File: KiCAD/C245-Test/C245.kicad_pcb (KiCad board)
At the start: 4 copper layers, 28 x 30 mm, 63 parts, among them J1 USB_C_Receptacle_USB2.0, J2 OLED_64x32, J3 C245, J5 DNP, Q1 SS8050, Q2 DMP3017SFG, SW1 key1, SW2 key2, U1 USBLC6-4SC6, U2 AP2204R-3.3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

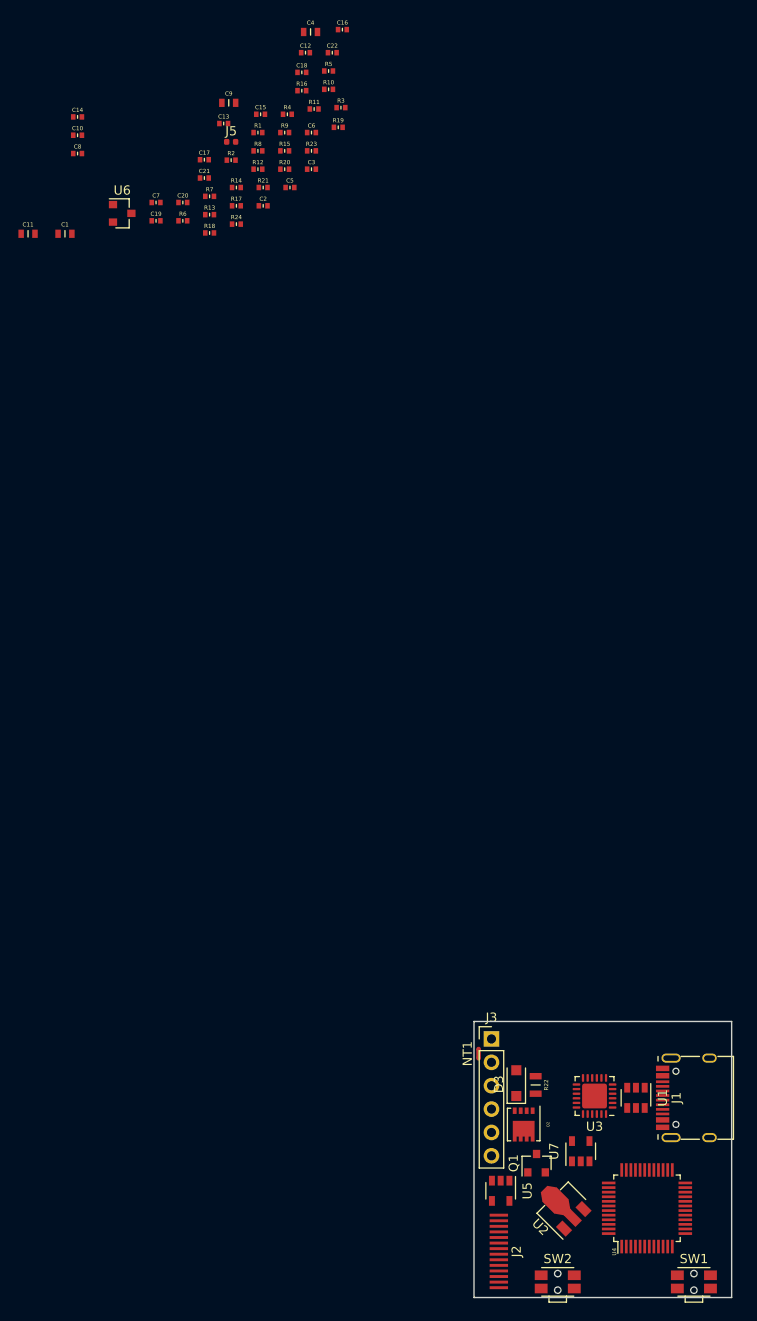
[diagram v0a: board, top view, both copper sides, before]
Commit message: added C245_Test
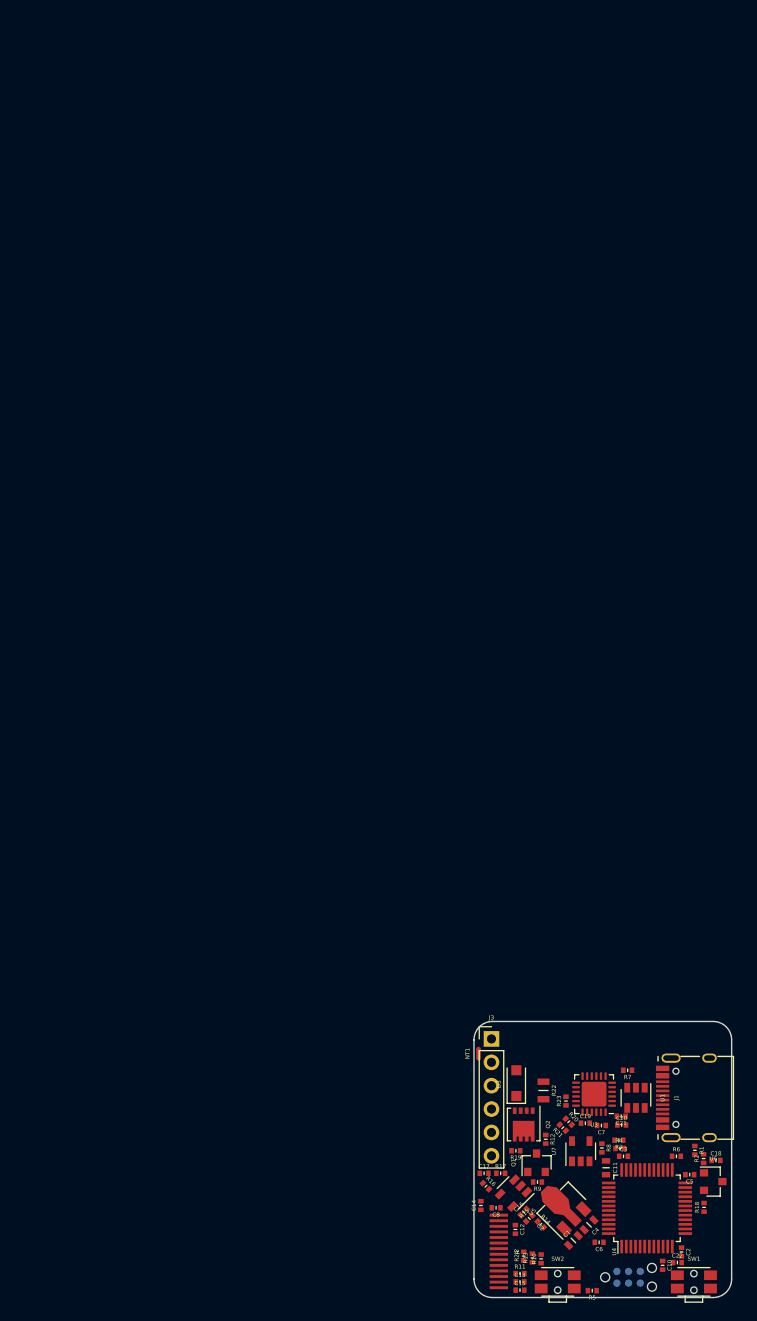
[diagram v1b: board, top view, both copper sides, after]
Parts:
- removed C9: 1μF 25V, otter:C_0603
- removed J5: DNP, Resistor_SMD:R_0402_1005Metric
- added P1: TC2030-CTX, otter:TC2030, B.Cu at (102.8, 117.8)
- moved C10 138.3 mm to (106.5, 116.5), turned to 270 degrees
- moved C22 136.7 mm to (108.1, 116.2)
- moved R5 135.6 mm to (98.8, 119.2), turned to 180 degrees
- moved C4 133.1 mm to (98.5, 112.1), turned to 225 degrees
- moved C15 130.9 mm to (91.0, 119.2)
- moved C16 130.0 mm to (91.4, 110.7), turned to 45 degrees
- moved C13 129.9 mm to (91.0, 118.3)
- moved C12 129.9 mm to (90.5, 112.6), turned to 270 degrees
- moved R10 129.2 mm to (93.3, 115.8), turned to 90 degrees
- moved R11 128.5 mm to (91.0, 117.4)
- moved C18 126.5 mm to (112.3, 105.1)
- moved C14 126.2 mm to (86.8, 110.0), turned to 90 degrees
- moved C6 124.6 mm to (99.6, 114.0), turned to 180 degrees
- moved U6 123.3 mm to (112.0, 107.4)
- moved C8 123.3 mm to (88.4, 110.2), turned to 180 degrees
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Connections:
- R5 pad 2: Net-(J5-Pad1) -> Net-(R5-Pad2)
- SW2 pad 2: Net-(SW2-Pad2) -> Net-(R5-Pad2)
- U4 pad 14: Net-(SW2-Pad2) -> Net-(U4-Pad14)
- U4 pad 2: Net-(U4-Pad2) -> Net-(R5-Pad2)
- U4 pad 44: Net-(J5-Pad1) -> Net-(R5-Pad2)
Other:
- outline, holes or cut-outs redrawn

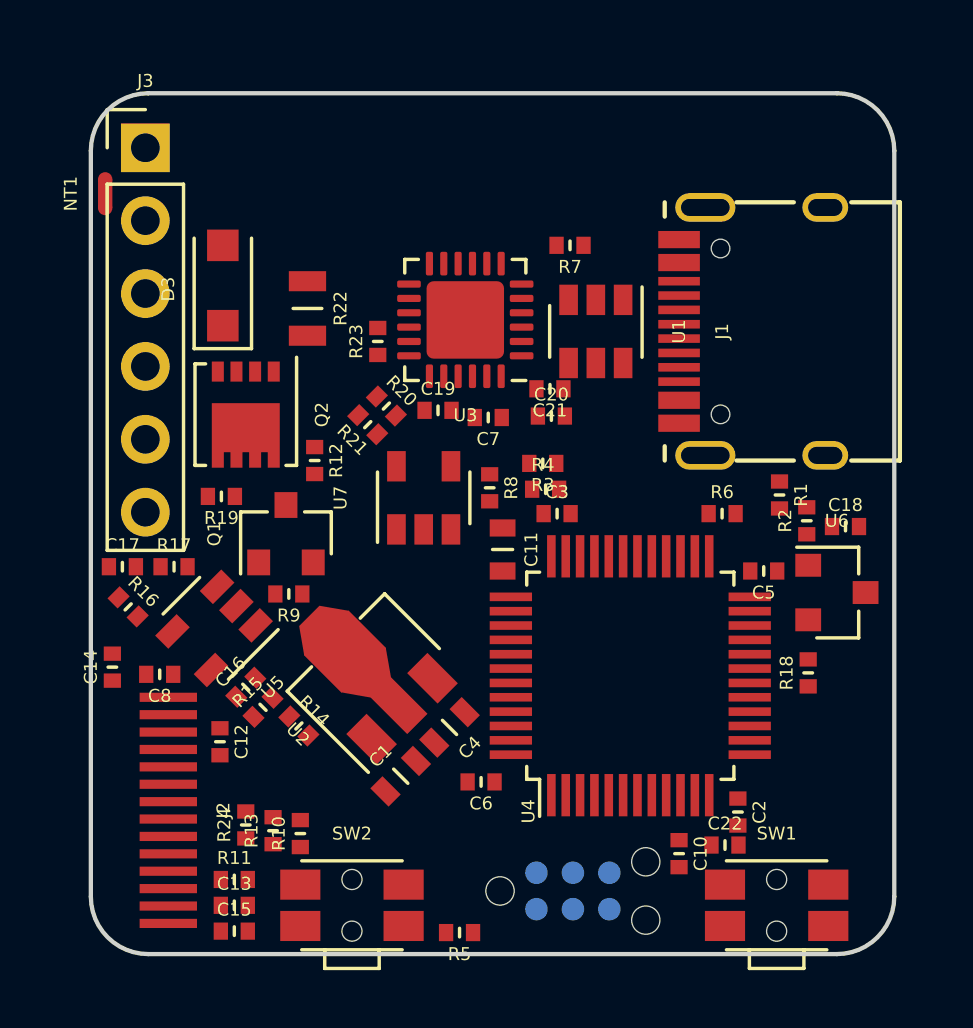
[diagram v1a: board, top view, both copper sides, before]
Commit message: added C245_Test
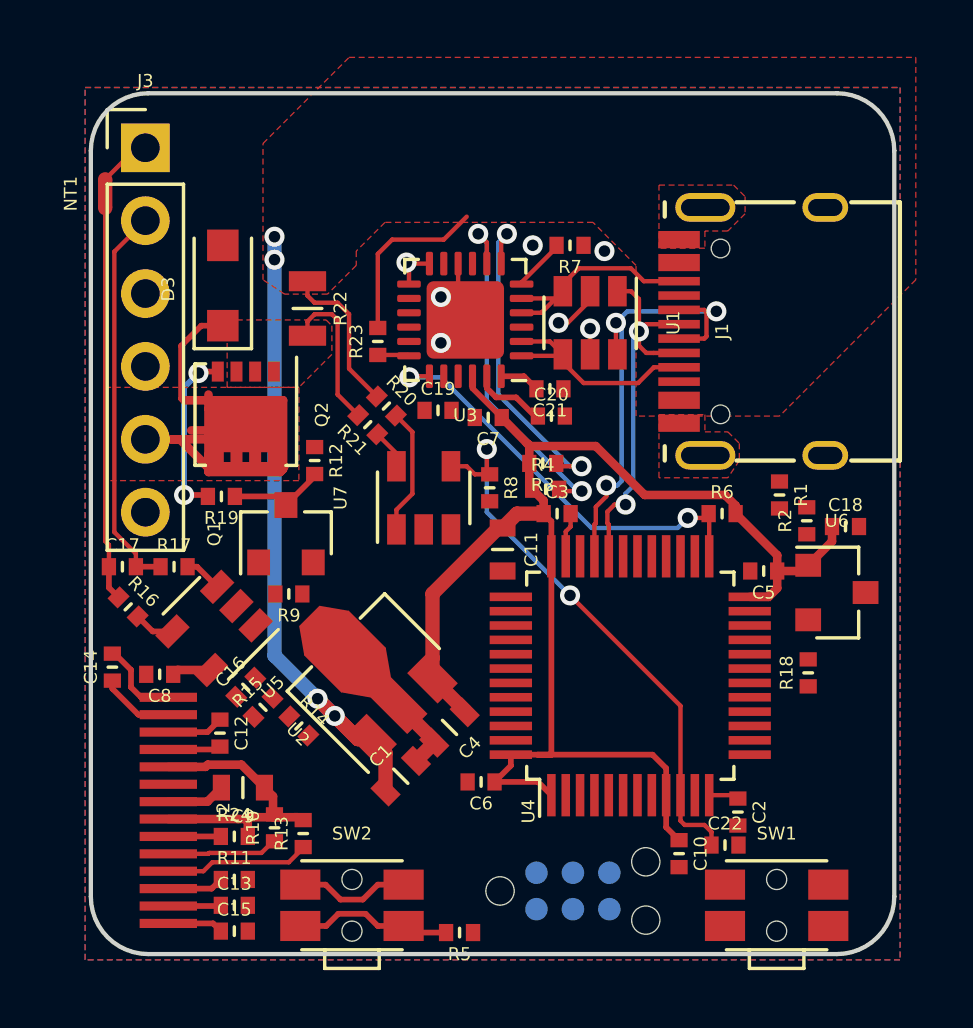
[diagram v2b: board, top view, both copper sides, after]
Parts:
- added C9: 1μF 25V, otter:C_0603, F.Cu at (91.3, 114.2)
- moved R13 1.05 mm to (93.4, 115.8)
- moved R10 0.92 mm to (92.4, 115.6)
- moved R24 0.57 mm to (91.0, 115.9), turned to 0 degrees
- moved U1 0.36 mm to (103.4, 98.0)
- moved C12 0.30 mm to (90.5, 112.3)
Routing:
- net +3V3: track 0.00 -> 68.1 mm, vias 0 -> 1
- net VBUS: track 0.00 -> 36.3 mm, vias 0 -> 4
- net Net-(D3-Pad1): track 0.00 -> 26.4 mm
- net IIN: track 0.00 -> 19.8 mm, vias 0 -> 2
- net USB_P: track 0.00 -> 16.8 mm, vias 0 -> 3
- net INT_N: track 0.00 -> 15.0 mm, vias 0 -> 2
- net USB_N: track 0.00 -> 14.0 mm, vias 0 -> 2
- net Net-(C17-Pad1): track 0.00 -> 13.8 mm
- net C245_JUNC: track 0.00 -> 13.7 mm
- net GND: track 0.00 -> 13.6 mm, vias 0 -> 6
- net SDA: track 0.00 -> 12.5 mm, vias 0 -> 2
- net SCL: track 0.00 -> 11.7 mm, vias 0 -> 2
- net CC2: track 0.00 -> 8.00 mm
- net CC1: track 0.00 -> 7.94 mm
- net Net-(Q2-Pad4): track 0.00 -> 6.00 mm, vias 0 -> 2
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- added copper zone on B.Cu, net GND
- added copper zone on F.Cu, net GND
- added copper zone on F.Cu, net Net-(D3-Pad1)
- added copper zone on F.Cu, net Net-(Q2-Pad1)
- added copper zone on F.Cu, net VBUS
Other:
- copper layers 4 -> 2

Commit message: finished routing C245_Test
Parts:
- moved R24 0.30 mm to (91.0, 115.6)
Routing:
- net +3V3: track 68.1 -> 100.0 mm, vias 1 -> 6
- net TTIP: track 0.00 -> 24.1 mm, vias 0 -> 2
- net SWCLK: track 0.00 -> 16.7 mm, vias 0 -> 1
- net PWM: track 0.00 -> 15.3 mm, vias 0 -> 2
- net SWDIO: track 0.00 -> 14.5 mm, vias 0 -> 1
- net VBUS: track 36.3 -> 50.3 mm, vias 4 -> 7
- net Net-(SW1-Pad2): track 0.00 -> 13.2 mm
- net Net-(R5-Pad2): track 5.53 -> 18.2 mm, vias 0 -> 2
- net UIN: track 1.05 -> 13.6 mm, vias 0 -> 2
- net OLED_SCL: track 3.88 -> 16.3 mm, vias 0 -> 2
- net OLED_SDA: track 5.07 -> 14.8 mm, vias 0 -> 2
- net SCL: track 11.7 -> 21.3 mm, vias 2 -> 3
- net SDA: track 12.5 -> 21.0 mm, vias 2 -> 3
- net Net-(C16-Pad1): track 1.43 -> 6.34 mm
- net GND: track 13.6 -> 18.2 mm, vias 6 -> 55
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
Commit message: finalized design
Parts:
- added G***: LOGO, otter:C245_silk, F.Cu at (98.4, 92.7)
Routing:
- net GND: vias 55 -> 56

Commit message: added silkscreen
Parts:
- moved G*** 0.56 mm to (97.8, 92.5)
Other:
- board text added: "*mau*"

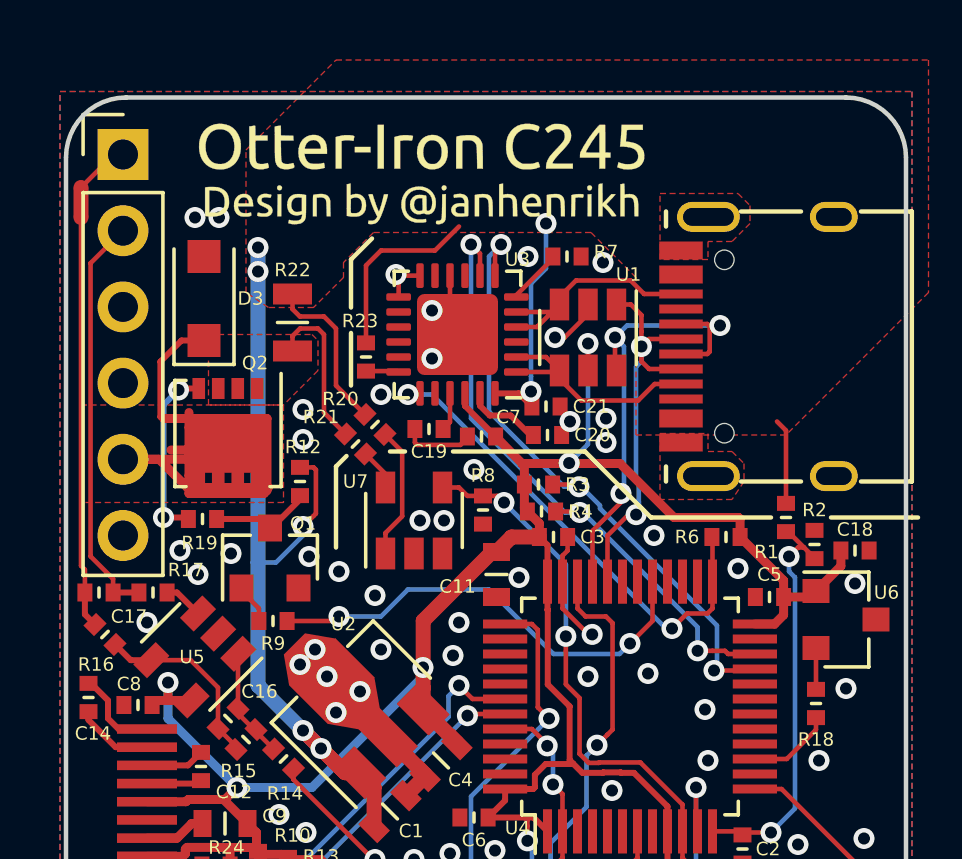
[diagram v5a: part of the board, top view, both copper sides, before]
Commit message: added connector pcb, added Gerber
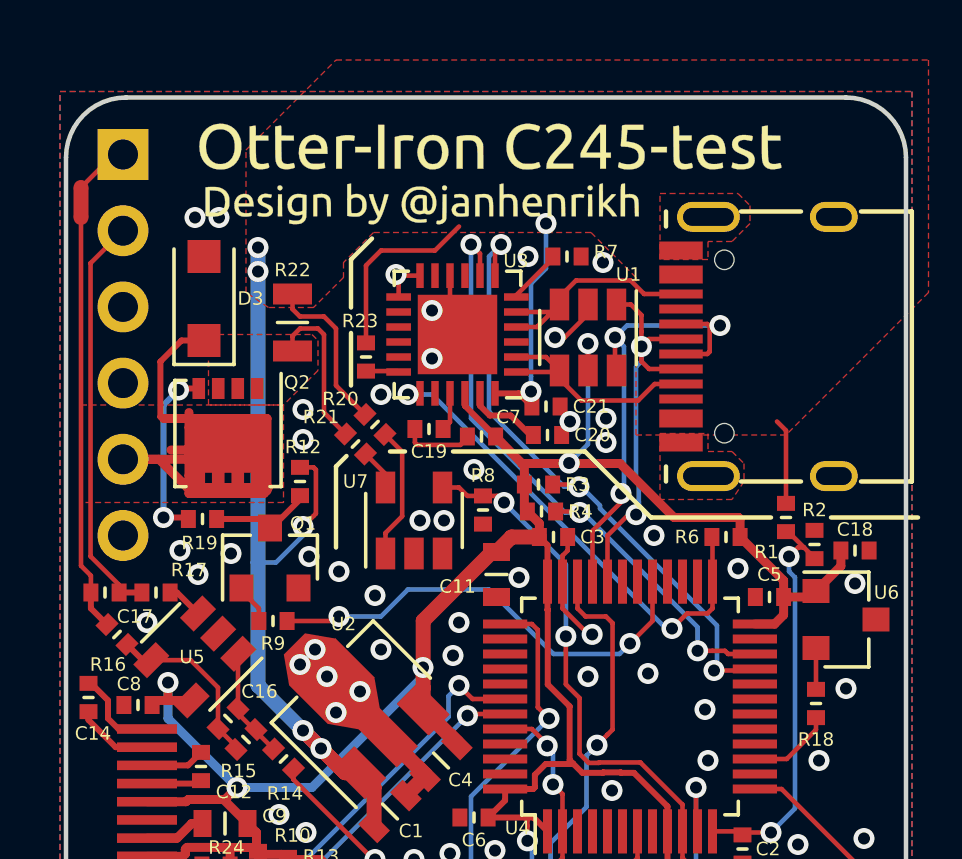
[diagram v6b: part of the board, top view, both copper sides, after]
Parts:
- U3: footprint Package_DFN_QFN:QFN-24-1EP_4x4mm_P0.5mm_EP2.7x2.7mm -> otter:QFN-24-1EP_4x4mm_P0.5mm_EP2.7x2.7mm
- moved G*** 2.30 mm to (100.2, 92.5)
- moved R16 0.40 mm to (87.7, 107.9)
- moved C17 0.20 mm to (87.3, 106.5)
- moved R17 0.10 mm to (89.0, 106.5)
